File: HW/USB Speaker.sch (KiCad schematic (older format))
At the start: 33 parts, among them J1 USB_OTG, U1 PCM2707C, Y1 12 MHz

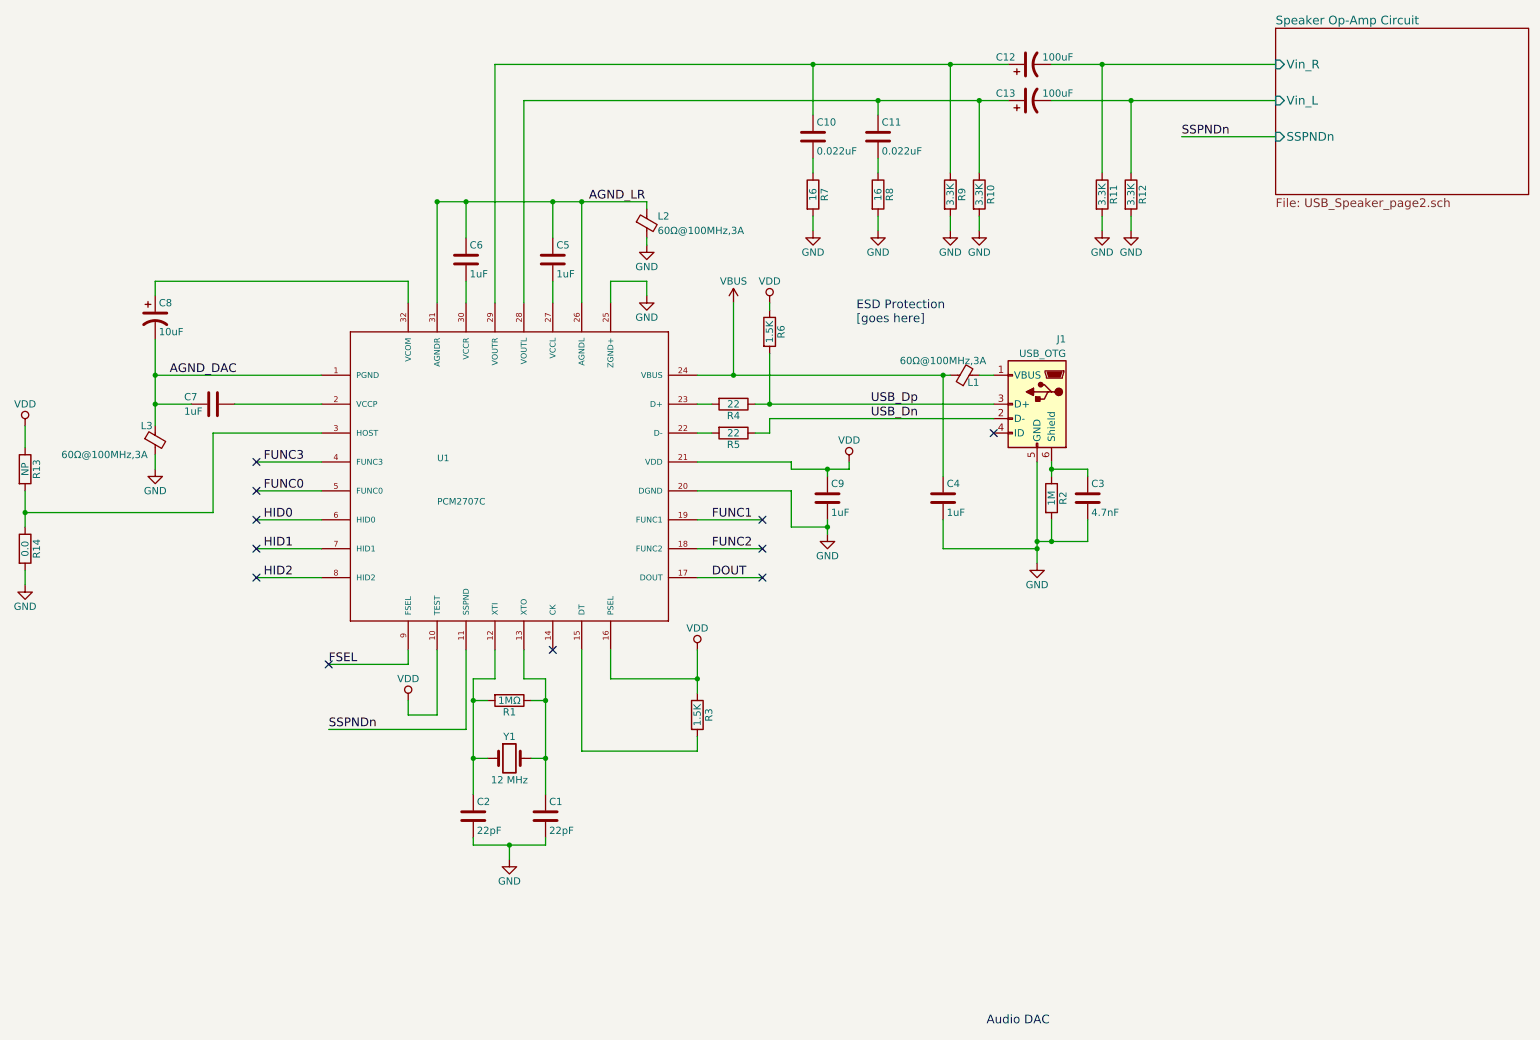
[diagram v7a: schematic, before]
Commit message: Basic battery power supply topology
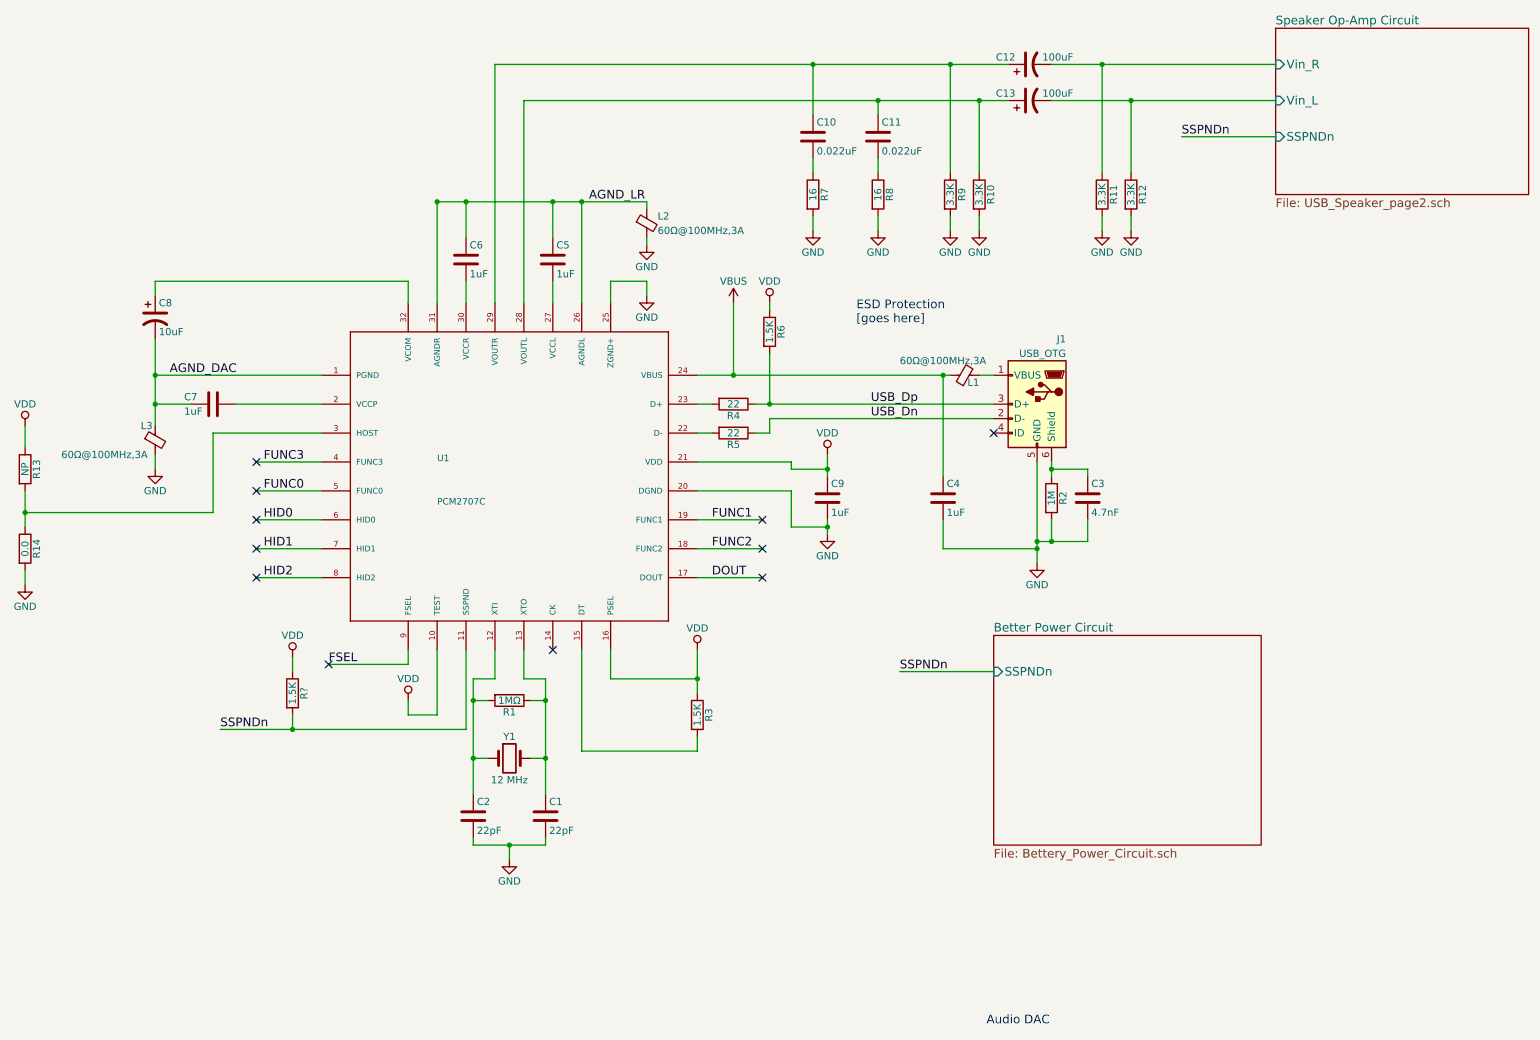
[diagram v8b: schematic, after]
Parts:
- added R?: 1.5K, symbol R
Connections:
- net SSPNDn: now also R?.2
- net VDD: now also R?.1
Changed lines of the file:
@@
 $Descr A4 11693 8268
 encoding utf-8
-Sheet 1 2
+Sheet 1 3
 Title ""
 Date ""
@@
 L VDD #PWR?
 U 1 1 5B1A1B5D
-P 6450 3600
-F 0 "#PWR?" H 6450 3450 50  0001 C CNN
-F 1 "VDD" H 6450 3750 50  0000 C CNN
-F 2 "" H 6450 3600 50  0001 C CNN
-F 3 "" H 6450 3600 50  0001 C CNN
-	1    6450 3600
+P 6300 3550
+F 0 "#PWR?" H 6300 3400 50  0001 C CNN
+F 1 "VDD" H 6300 3700 50  0000 C CNN
+F 2 "" H 6300 3550 50  0001 C CNN
+F 3 "" H 6300 3550 50  0001 C CNN
+	1    6300 3550
 	1    0    0    -1
 $EndComp
@@
 	3850 5100 4000 5100
 Wire Wire Line
-	3850 5100 3850 5900
+	3850 5100 3850 5250
+Wire Wire Line
+	3850 5250 3850 5650
+Wire Wire Line
+	3850 5650 3850 5900
 Wire Wire Line
 	4350 5650 4250 5650
@@
 	4100 6350 4100 6250
 Wire Wire Line
-	3850 6250 4350 6250
+	3850 6250 4100 6250
+Wire Wire Line
+	4100 6250 4350 6250
 Wire Wire Line
 	3850 6250 3850 6200
@@
 Connection ~ 4100 6250
 Wire Wire Line
-	4350 5100 4350 5900
-Wire Wire Line
-	7750 3600 7750 4300
-Wire Wire Line
-	7750 4150 8100 4150
-Wire Wire Line
-	7850 3600 7850 3700
+	4350 5100 4350 5250
+Wire Wire Line
+	4350 5250 4350 5650
+Wire Wire Line
+	4350 5650 4350 5900
+Wire Wire Line
+	7750 3600 7750 4150
+Wire Wire Line
+	7750 4150 7750 4200
+Wire Wire Line
+	7750 4200 7750 4300
+Wire Wire Line
+	7750 4150 7850 4150
+Wire Wire Line
+	7850 4150 8100 4150
+Wire Wire Line
+	7850 3600 7850 3650
+Wire Wire Line
+	7850 3650 7850 3700
 Wire Wire Line
 	7850 4150 7850 4000
@@
 	7450 3000 7350 3000
 Wire Wire Line
-	5400 3000 7150 3000
+	5400 3000 5650 3000
+Wire Wire Line
+	5650 3000 7100 3000
+Wire Wire Line
+	7100 3000 7150 3000
 Wire Wire Line
 	7100 3700 7100 3000
@@
 	7100 4200 7750 4200
 Wire Wire Line
-	3600 1800 5050 1800
+	3600 1800 3800 1800
+Wire Wire Line
+	3800 1800 4400 1800
+Wire Wire Line
+	4400 1800 4600 1800
+Wire Wire Line
+	4600 1800 5050 1800
 Wire Wire Line
 	3600 1800 3600 2500
@@
 Connection ~ 3800 1800
 Wire Wire Line
-	1650 2750 1650 3350
+	1650 2750 1650 3000
+Wire Wire Line
+	1650 3000 1650 3200
+Wire Wire Line
+	1650 3200 1650 3350
 Wire Wire Line
 	1900 3200 1650 3200
@@
 	4800 5100 5400 5100
 Wire Wire Line
-	5400 4900 5400 5200
+	5400 4900 5400 5100
+Wire Wire Line
+	5400 5100 5400 5200
 Wire Wire Line
 	2200 3200 2800 3200
@@
 	5400 5600 5400 5500
 Wire Wire Line
-	6450 3650 6450 3600
-Wire Wire Line
-	6050 3650 6450 3650
+	6300 3550 6300 3650
 Wire Wire Line
 	6300 3650 6300 3700
+Wire Wire Line
+	6300 3650 6050 3650
 Wire Wire Line
 	6050 3650 6050 3600
@@
 	6050 3800 6050 4050
 Wire Wire Line
-	6300 4000 6300 4100
+	6300 4000 6300 4050
+Wire Wire Line
+	6300 4050 6300 4100
 Wire Wire Line
 	6050 4050 6300 4050
@@
 	5400 3400 5500 3400
 Wire Wire Line
-	5800 3200 7450 3200
+	5800 3200 5900 3200
+Wire Wire Line
+	5900 3200 7450 3200
 Wire Wire Line
 	5800 3400 5900 3400
@@
 	4000 850  4000 2500
 Wire Wire Line
-	4000 850  7550 850
+	4000 850  6200 850
+Wire Wire Line
+	6200 850  7150 850
+Wire Wire Line
+	7150 850  7550 850
 Wire Wire Line
 	4200 1100 4200 2500
 Wire Wire Line
-	4200 1100 7550 1100
-Wire Wire Line
-	7850 850  9400 850
-Wire Wire Line
-	7850 1100 9400 1100
+	4200 1100 6650 1100
+Wire Wire Line
+	6650 1100 7350 1100
+Wire Wire Line
+	7350 1100 7550 1100
+Wire Wire Line
+	7850 850  8200 850
+Wire Wire Line
+	8200 850  9400 850
+Wire Wire Line
+	7850 1100 8400 1100
+Wire Wire Line
+	8400 1100 9400 1100
 Wire Wire Line
 	6200 1200 6200 850
@@
 	5400 4400 5850 4400
 Wire Wire Line
-	3800 4900 3800 5450
-Wire Wire Line
-	3800 5450 2850 5450
+	3800 5450 3800 4900
+Wire Wire Line
+	2100 5450 2600 5450
+Wire Wire Line
+	2600 5450 3800 5450
 Wire Wire Line
 	2800 3400 2050 3400
@@
 	2050 3950 750  3950
 Wire Wire Line
-	750  3800 750  4050
+	750  3800 750  3950
+Wire Wire Line
+	750  3950 750  4050
 $Comp
 L R R13
@@
 	5650 2500 5650 3000
 Connection ~ 5650 3000
-Text Label 2850 5450 0    60   ~ 0
+Text Label 2100 5450 0    60   ~ 0
 SSPNDn
 Wire Wire Line
@@
 Text Label 8750 1350 0    60   ~ 0
 SSPNDn
+$Sheet
+S 7450 4800 1850 1450
+U 5B317E48
+F0 "Better Power Circuit" 60
+F1 "Bettery_Power_Circuit.sch" 60
+F2 "SSPNDn" I L 7450 5050 60
+$EndSheet
+$Comp
+L R R?
+U 1 1 5B3333BD
+P 2600 5200
+F 0 "R?" V 2680 5200 50  0000 C CNN
+F 1 "1.5K" V 2600 5200 50  0000 C CNN
+F 2 "" V 2530 5200 50  0001 C CNN
+F 3 "" H 2600 5200 50  0001 C CNN
+	1    2600 5200
+	1    0    0    -1
+$EndComp
+$Comp
+L VDD #PWR?
+U 1 1 5B33365A
+P 2600 4950
+F 0 "#PWR?" H 2600 4800 50  0001 C CNN
+F 1 "VDD" H 2600 5100 50  0000 C CNN
+F 2 "" H 2600 4950 50  0001 C CNN
+F 3 "" H 2600 4950 50  0001 C CNN
+	1    2600 4950
+	1    0    0    -1
+$EndComp
+Wire Wire Line
+	2600 5050 2600 4950
+Wire Wire Line
+	2600 5350 2600 5450
+Connection ~ 2600 5450
+Wire Wire Line
+	7450 5050 6800 5050
+Text Label 6800 5050 0    60   ~ 0
+SSPNDn
 $EndSCHEMATC
